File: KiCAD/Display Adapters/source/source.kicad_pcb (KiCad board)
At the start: 4 copper layers, 38 x 29.6 mm, 5 parts, among them J1 20455-040E-76, J2 XT30PW_2_2_-M.G.B, J3 G46M2013201AWEU

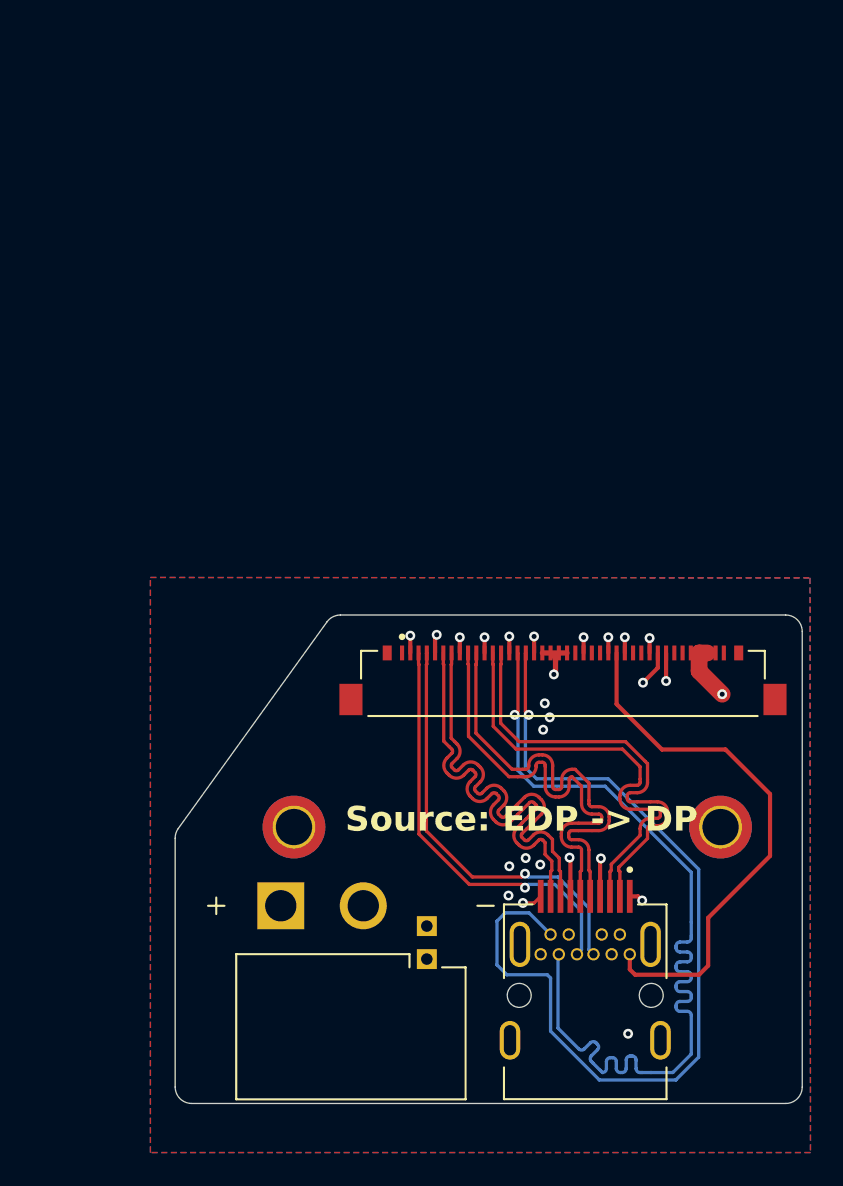
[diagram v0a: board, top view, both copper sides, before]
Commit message: use full sized dp instead
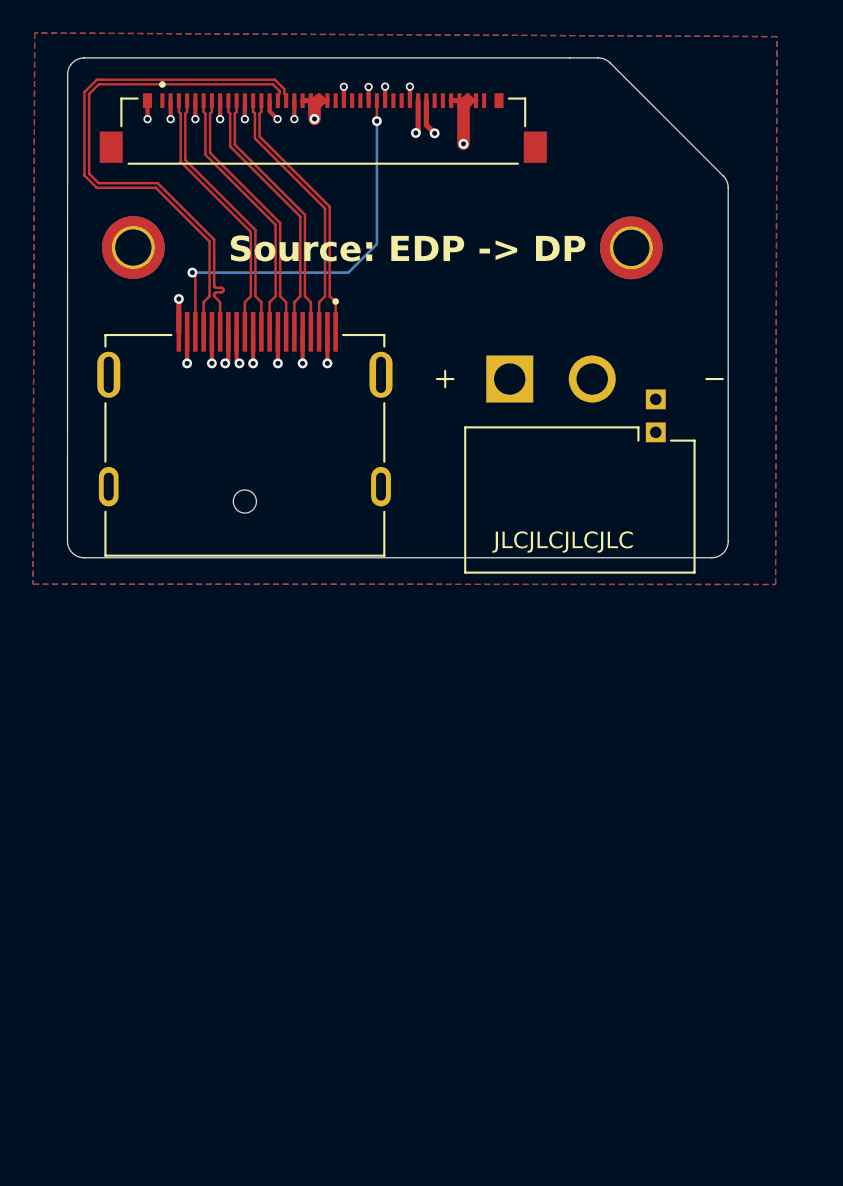
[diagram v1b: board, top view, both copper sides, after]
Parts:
- J2: value XT30PW_2_2_-M.G.B -> 47272-0001; footprint SnapEDA:AMASS_XT30PW_2_2_-M.G.B -> SnapEDA:MOLEX_47272-0001
- J3: value G46M2013201AWEU -> XT30PW_2_2_-M.G.B; footprint SnapEDA:AMPHENOL_G46M2013201AWEU -> SnapEDA:AMASS_XT30PW_2_2_-M.G.B
- moved J1 36.5 mm to (130.5, 58.0)
- moved H1 36.4 mm to (119.0, 65.0)
- moved H2 35.5 mm to (149.2, 65.0)
- moved J3 30.0 mm to (146.1, 80.3)
- moved J2 29.3 mm to (125.8, 83.7)
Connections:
- J2 pad S1: BLK_PWM_LCD -> GND
- J2 pad S2: BLK_OFF_N -> GND
- J3 pad S1: GND -> BLK_OFF_N
- J3 pad S2: GND -> BLK_PWM_LCD
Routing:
- net +5V: track 64.6 -> 19.6 mm
- net AUX_N: track 55.8 -> 33.3 mm, vias 1 -> 0
- net AUX_P: track 55.5 -> 33.3 mm, vias 1 -> 0
- net 2_EDP_TX_N: track 26.9 -> 16.0 mm
- net BLK_OFF_N: track 23.5 -> 34.4 mm
- net 0_EDP_TX_P: track 26.8 -> 16.0 mm
- net 0_EDP_TX_N: track 26.8 -> 16.0 mm
- net 2_EDP_TX_P: track 26.8 -> 16.0 mm
- net 1_EDP_TX_N: track 26.7 -> 16.0 mm
- net 1_EDP_TX_P: track 26.7 -> 16.0 mm
- net 3_EDP_TX_P: track 25.7 -> 16.0 mm, vias 1 -> 0
- net 3_EDP_TX_N: track 25.7 -> 16.0 mm, vias 1 -> 0
- net +3.3V: track 13.1 -> 4.74 mm, vias 1 -> 2
- net EDP_HPD: track 32.6 -> 24.3 mm, vias 0 -> 2
- net BLK_PWM_LCD: track 25.8 -> 32.7 mm
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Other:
- board size 38 x 29.6 mm -> 40 x 30.3 mm
- board text added: "JLCJLCJLCJLC"
- board text added: "chinh4"
